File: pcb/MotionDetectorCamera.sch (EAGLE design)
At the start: 127 parts, among them J2 S-MOUNT-LENS-HOLDER, U1 LATTICE-ICE40HX4K-BG121, U10 NXP-NTB0102, U11 ON-NLAS3157, U12 ON-NLAS3157, U13 STM-STM32F730, U2 TI-TPS6280XYKAR, U3 MICROSD-SOCKET, U4 TI-TPS6280XYKAR, U5 W989D6DBGX6I, U6 TI-TPS63805YFFR, U8 ON-AR0330CS1C12SPKA0, U9 TI-TMUX1574, X1 SITIME-SIT8021, X2 SITIME-SIT8021

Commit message: Commit before renaming ICE_PRG lines
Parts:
- C56: device EagleLibrary:CAPACITOR0402 -> EagleLibrary:CAPACITOR0805; MFG (none) -> Walsin; PN (none) -> 0805X475M250CT
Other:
- moved on the sheet: C22, H2, J2, LED0, LED1, LED2, LED3, R14, R16, R20, R22, TP6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

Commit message: Routing progress
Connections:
- removed net ICE_PRG_CDONE: H2.5, U1E.CDONE_K8
- removed net ICE_PRG_CLK: H2.2, U1E.SPI_SCK_L10
- removed net ICE_PRG_CRST_: H2.10, R5.2, U1E.CRESET_B_L9
- removed net ICE_PRG_CS_: H2.3, U1E.SPI_SS_B_K10
- removed net ICE_PRG_DI: H2.1, U1E.SPI_SI_J9
- removed net ICE_PRG_DO: H2.4, U1E.SPI_SO_K9
- removed net STM_SPI_CLK: U13B.PB2_M6
- removed net STM_SPI_CS_: U13B.PB6_B6
- removed net STM_SPI_D0: U13C.PC9_F14
- removed net STM_SPI_D1: U13C.PC10_B14
- removed net STM_SPI_D2: U13E.PE2_A2
- removed net STM_SPI_D3: U13F.PF6_K2
- removed net STM_SPI_D4: U13H.PH2_F4
- removed net STM_SPI_D5: U13H.PH3_G4
- removed net STM_SPI_D6: U13G.PG9_C10
- removed net STM_SPI_D7: U13G.PG14_A7
- new net ICE_CDONE: H2.5, U13I.PI7_C2, U1E.CDONE_K8
- new net ICE_CRST_: H2.10, R5.2, U13I.PI6_C3, U1E.CRESET_B_L9
- new net ICE_SPI_CLK: H2.2, U13B.PB2_M6, U1E.SPI_SCK_L10
- new net ICE_SPI_CS_: H2.3, U13B.PB6_B6, U1E.SPI_SS_B_K10
- new net ICE_SPI_D0: H2.1, U13C.PC9_F14, U1E.SPI_SI_J9
- new net ICE_SPI_D1: H2.4, U13C.PC10_B14, U1E.SPI_SO_K9
- new net ICE_SPI_D2: U13E.PE2_A2, U1C.J8
- new net ICE_SPI_D3: U13F.PF6_K2, U1C.L7
- new net ICE_SPI_D4: U13H.PH2_F4, U1C.J7
- new net ICE_SPI_D5: U13H.PH3_G4, U1C.K7
- new net ICE_SPI_D6: U13G.PG9_C10, U1C.H7
- new net ICE_SPI_D7: U13G.PG14_A7, U1C.L8
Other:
- moved on the sheet: C67, C68, R28, R29, R30, R31, U13J

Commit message: Layout progress
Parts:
- removed LED0: LED, EagleLibrary:LED
- removed R29, R30: 10k, EagleLibrary:RESISTOR0402
- added LED4: LED, EagleLibrary:LED
- C56: device EagleLibrary:CAPACITOR0805 -> EagleLibrary:CAPACITOR0603; MFG Walsin -> Taiyo Yuden; PN 0805X475M250CT -> LMK107BJ475KA-T
- C57, C58, C67: MFG (none) -> AVX; PN (none) -> 0402ZD225MAT2A
- C60, C66: MFG (none) -> Taiyo Yuden; PN (none) -> EMK105BJ105MVHF
- H1: value WURTH-61201021621 -> HEADER-2X5; device EagleLibrary:WURTH-61201021621 -> EagleLibrary:HEADER-2X5
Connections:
- net N$15 renamed STM_BOOT
- net N$19 renamed STM_RST_
- removed net N$22: R29.2, U13J.PDR_ON_C6
- removed net N$24: R30.2, U13J.BYPASS_REG_L4
- net 1V8: now also U13J.PDR_ON_C6; no longer R29.1
- net GND: now also U13J.BYPASS_REG_L4; no longer R30.1
- net ICE_LED0: now also LED1.A; no longer LED0.A
- net ICE_LED1: now also LED2.A; no longer LED1.A
- net ICE_LED2: now also LED3.A; no longer LED2.A
- net ICE_LED3: now also LED4.A; no longer LED3.A
- net N$23: now also LED1.C; no longer LED0.C
- net N$26: now also LED2.C; no longer LED1.C
- net N$29: now also LED3.C; no longer LED2.C
- net N$31: now also LED4.C; no longer LED3.C
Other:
- moved on the sheet: C68, LED1, LED2, LED3, LED5, LED6, LED7, LED8, R15, R17, R31, R32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

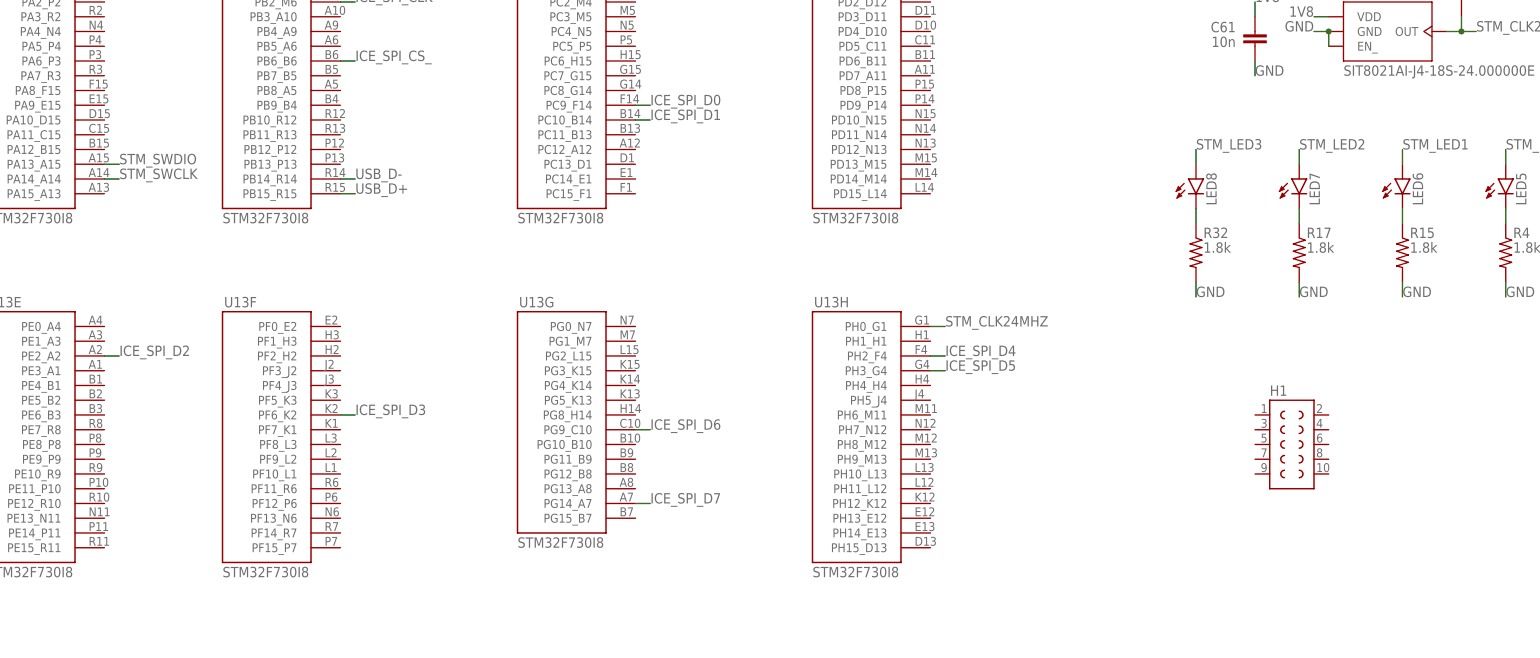
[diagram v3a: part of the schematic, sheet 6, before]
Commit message: Wired up STM32 LEDs
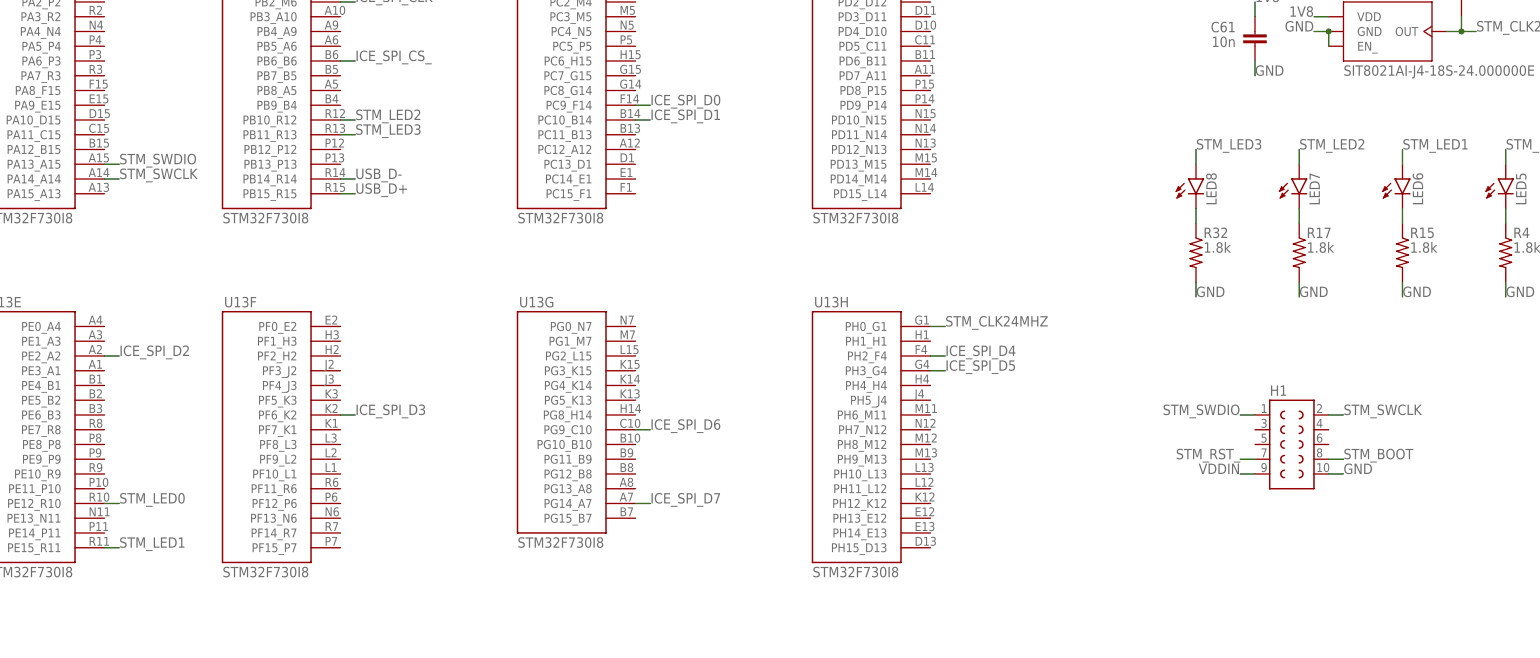
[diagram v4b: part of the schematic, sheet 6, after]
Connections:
- net GND: now also H1.10
- net STM_BOOT: now also H1.8
- net STM_LED0: now also U13E.PE12_R10
- net STM_LED1: now also U13E.PE15_R11
- net STM_LED2: now also U13B.PB10_R12
- net STM_LED3: now also U13B.PB11_R13
- net STM_RST_: now also H1.7
- net STM_SWCLK: now also H1.2
- net STM_SWDIO: now also H1.1
- net VDDIN: now also H1.9
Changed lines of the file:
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@@
 <label x="81.28" y="-142.24" size="1.778" layer="95"/>
+</segment>
+<segment>
+<pinref part="H1" gate="G$1" pin="10"/>
+<wire x1="238.76" y1="-99.06" x2="241.3" y2="-99.06" width="0.1524" layer="91"/>
+<label x="241.3" y="-99.06" size="1.778" layer="95"/>
 </segment>
 </net>
@@
 <label x="101.6" y="-144.78" size="1.778" layer="95"/>
 </segment>
+<segment>
+<pinref part="H1" gate="G$1" pin="7"/>
+<wire x1="226.06" y1="-96.52" x2="223.52" y2="-96.52" width="0.1524" layer="91"/>
+<label x="223.52" y="-96.52" size="1.778" layer="95" align="bottom-right"/>
+</segment>
 </net>
 <net name="STM_BOOT" class="0">
@@
 <junction x="116.84" y="-139.7"/>
 </segment>
+<segment>
+<pinref part="H1" gate="G$1" pin="8"/>
+<wire x1="238.76" y1="-96.52" x2="241.3" y2="-96.52" width="0.1524" layer="91"/>
+<label x="241.3" y="-96.52" size="1.778" layer="95"/>
+</segment>
 </net>
 <net name="USB_D-" class="0">
@@
 <label x="30.48" y="-45.72" size="1.778" layer="95"/>
 </segment>
+<segment>
+<pinref part="H1" gate="G$1" pin="1"/>
+<wire x1="226.06" y1="-88.9" x2="223.52" y2="-88.9" width="0.1524" layer="91"/>
+<label x="223.52" y="-88.9" size="1.778" layer="95" align="bottom-right"/>
+</segment>
 </net>
 <net name="STM_SWCLK" class="0">
@@
 <wire x1="27.94" y1="-48.26" x2="30.48" y2="-48.26" width="0.1524" layer="91"/>
 <label x="30.48" y="-48.26" size="1.778" layer="95"/>
+</segment>
+<segment>
+<pinref part="H1" gate="G$1" pin="2"/>
+<wire x1="238.76" y1="-88.9" x2="241.3" y2="-88.9" width="0.1524" layer="91"/>
+<label x="241.3" y="-88.9" size="1.778" layer="95"/>
 </segment>
 </net>
@@
 <label x="269.24" y="-43.18" size="1.778" layer="95"/>
 </segment>
+<segment>
+<pinref part="U13" gate="E" pin="PE12_R10"/>
+<wire x1="27.94" y1="-104.14" x2="30.48" y2="-104.14" width="0.1524" layer="91"/>
+<label x="30.48" y="-104.14" size="1.778" layer="95"/>
+</segment>
 </net>
 <net name="STM_LED1" class="0">
@@
 <label x="251.46" y="-43.18" size="1.778" layer="95"/>
 </segment>
+<segment>
+<pinref part="U13" gate="E" pin="PE15_R11"/>
+<wire x1="27.94" y1="-111.76" x2="30.48" y2="-111.76" width="0.1524" layer="91"/>
+<label x="30.48" y="-111.76" size="1.778" layer="95"/>
+</segment>
 </net>
 <net name="STM_LED2" class="0">
@@
 <label x="233.68" y="-43.18" size="1.778" layer="95"/>
 </segment>
+<segment>
+<pinref part="U13" gate="B" pin="PB10_R12"/>
+<wire x1="68.58" y1="-38.1" x2="71.12" y2="-38.1" width="0.1524" layer="91"/>
+<label x="71.12" y="-38.1" size="1.778" layer="95"/>
+</segment>
 </net>
 <net name="STM_LED3" class="0">
@@
 <label x="215.9" y="-43.18" size="1.778" layer="95"/>
 </segment>
+<segment>
+<pinref part="U13" gate="B" pin="PB11_R13"/>
+<wire x1="68.58" y1="-40.64" x2="71.12" y2="-40.64" width="0.1524" layer="91"/>
+<label x="71.12" y="-40.64" size="1.778" layer="95"/>
+</segment>
 </net>
 <net name="ICE_CDONE" class="0">
@@
 </segment>
 </net>
+<net name="VDDIN" class="0">
+<segment>
+<pinref part="H1" gate="G$1" pin="9"/>
+<wire x1="226.06" y1="-99.06" x2="223.52" y2="-99.06" width="0.1524" layer="91"/>
+<label x="223.52" y="-99.06" size="1.778" layer="95" align="bottom-right"/>
+</segment>
+</net>

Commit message: Laying out SD card in progress
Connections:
- net ICE_SD_CLK: now also U1C.L3
- net ICE_SD_DAT0: now also U1C.L2; no longer U1C.L3
- net ICE_SD_DAT1: now also U1C.L1; no longer U1C.K4
- net ICE_SD_DAT2: now also U1C.K4; no longer U1C.L1
- net ICE_SD_DAT3: no longer U1C.L2
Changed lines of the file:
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@@
 <label x="152.4" y="30.48" size="1.778" layer="95"/>
 </segment>
-</net>
-<net name="ICE_SD_CMD" class="0">
-<segment>
-<pinref part="U1" gate="C" pin="K3"/>
-<wire x1="149.86" y1="48.26" x2="152.4" y2="48.26" width="0.1524" layer="91"/>
-<label x="152.4" y="48.26" size="1.778" layer="95"/>
-</segment>
-</net>
-<net name="ICE_SD_DAT0" class="0">
 <segment>
 <pinref part="U1" gate="C" pin="L3"/>
 <wire x1="149.86" y1="60.96" x2="152.4" y2="60.96" width="0.1524" layer="91"/>
 <label x="152.4" y="60.96" size="1.778" layer="95"/>
-</segment>
-</net>
-<net name="ICE_SD_DAT1" class="0">
-<segment>
-<pinref part="U1" gate="C" pin="K4"/>
-<wire x1="149.86" y1="45.72" x2="152.4" y2="45.72" width="0.1524" layer="91"/>
-<label x="152.4" y="45.72" size="1.778" layer="95"/>
-</segment>
-</net>
-<net name="ICE_SD_DAT2" class="0">
-<segment>
-<pinref part="U1" gate="C" pin="L1"/>
-<wire x1="149.86" y1="66.04" x2="152.4" y2="66.04" width="0.1524" layer="91"/>
-<label x="152.4" y="66.04" size="1.778" layer="95"/>
-</segment>
-</net>
-<net name="ICE_SD_DAT3" class="0">
-<segment>
-<pinref part="U1" gate="C" pin="L2"/>
-<wire x1="149.86" y1="63.5" x2="152.4" y2="63.5" width="0.1524" layer="91"/>
-<label x="152.4" y="63.5" size="1.778" layer="95"/>
 </segment>
 </net>
@@
 </segment>
 </net>
+<net name="ICE_SD_DAT1" class="0">
+<segment>
+<pinref part="U1" gate="C" pin="L1"/>
+<wire x1="149.86" y1="66.04" x2="152.4" y2="66.04" width="0.1524" layer="91"/>
+<label x="152.4" y="66.04" size="1.778" layer="95"/>
+</segment>
+</net>
+<net name="ICE_SD_DAT2" class="0">
+<segment>
+<pinref part="U1" gate="C" pin="K4"/>
+<wire x1="149.86" y1="45.72" x2="152.4" y2="45.72" width="0.1524" layer="91"/>
+<label x="152.4" y="45.72" size="1.778" layer="95"/>
+</segment>
+</net>
+<net name="ICE_SD_DAT0" class="0">
+<segment>
+<pinref part="U1" gate="C" pin="L2"/>
+<wire x1="149.86" y1="63.5" x2="152.4" y2="63.5" width="0.1524" layer="91"/>
+<label x="152.4" y="63.5" size="1.778" layer="95"/>
+</segment>
+</net>
+<net name="ICE_SD_CMD" class="0">
+<segment>
+<pinref part="U1" gate="C" pin="K3"/>
+<wire x1="149.86" y1="48.26" x2="152.4" y2="48.26" width="0.1524" layer="91"/>
+<label x="152.4" y="48.26" size="1.778" layer="95"/>
+</segment>
+</net>

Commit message: Layout progress
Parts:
- added C30, C31, C62, C63, C64: 100n, EagleLibrary:CAPACITOR0402
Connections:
- net 1V8: now also C30.1
- net 2V8: now also C31.1, C62.1, C63.1, C64.1
- net GND: now also C30.2, C31.2, C62.2, C63.2, C64.2
- net ICE_SD_CLK: now also U1C.K3; no longer U1C.J5, U1C.L3
- net ICE_SD_CMD: now also U1C.L3; no longer U1C.K3
- net ICE_SD_DAT2: now also U1C.L4, U9.S4A; no longer U1C.K4, U9.S3A
- net ICE_SD_DAT3: now also U1C.K4, U9.S3A; no longer U9.S4A
- net ICE_SD_INIT: now also U1C.L5
- net N$17: now also U9.S4B; no longer U9.S3B
- net N$21: now also U9.S3B; no longer U9.S4B
- net SD_DAT0: now also U9.D2; no longer U9.D1
- net SD_DAT1: now also U9.D1; no longer U9.D2
- net SD_DAT2: now also U9.D4; no longer U9.D3
- net SD_DAT3: now also U9.D3; no longer U9.D4
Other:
- moved on the sheet: C19, C20, R26, R27, U3

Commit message: Layout progress
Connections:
- net ICE_SD_CLK: now also U1C.K4; no longer U1C.K3
- net ICE_SD_DAT1: now also U1C.K3; no longer U1C.L1
- net ICE_SD_DAT2: now also U1C.L5; no longer U1C.L4
- net ICE_SD_DAT3: now also U1C.L4; no longer U1C.K4
- net ICE_SD_INIT: now also U1C.L1; no longer U1C.L5
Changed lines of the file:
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@@
 <net name="ICE_SD_CLK" class="0">
 <segment>
-<pinref part="U1" gate="C" pin="K3"/>
-<wire x1="149.86" y1="48.26" x2="152.4" y2="48.26" width="0.1524" layer="91"/>
-<label x="152.4" y="48.26" size="1.778" layer="95"/>
+<wire x1="149.86" y1="45.72" x2="152.4" y2="45.72" width="0.1524" layer="91"/>
+<label x="152.4" y="45.72" size="1.778" layer="95"/>
+<pinref part="U1" gate="C" pin="K4"/>
 </segment>
 </net>
@@
 <net name="ICE_SD_DAT1" class="0">
 <segment>
-<pinref part="U1" gate="C" pin="L1"/>
-<wire x1="149.86" y1="66.04" x2="152.4" y2="66.04" width="0.1524" layer="91"/>
-<label x="152.4" y="66.04" size="1.778" layer="95"/>
+<wire x1="149.86" y1="48.26" x2="152.4" y2="48.26" width="0.1524" layer="91"/>
+<label x="152.4" y="48.26" size="1.778" layer="95"/>
+<pinref part="U1" gate="C" pin="K3"/>
 </segment>
 </net>
 <net name="ICE_SD_DAT0" class="0">
 <segment>
-<pinref part="U1" gate="C" pin="L2"/>
 <wire x1="149.86" y1="63.5" x2="152.4" y2="63.5" width="0.1524" layer="91"/>
 <label x="152.4" y="63.5" size="1.778" layer="95"/>
+<pinref part="U1" gate="C" pin="L2"/>
 </segment>
 </net>
 <net name="ICE_SD_CMD" class="0">
 <segment>
-<pinref part="U1" gate="C" pin="L3"/>
 <wire x1="149.86" y1="60.96" x2="152.4" y2="60.96" width="0.1524" layer="91"/>
 <label x="152.4" y="60.96" size="1.778" layer="95"/>
+<pinref part="U1" gate="C" pin="L3"/>
 </segment>
 </net>
 <net name="ICE_SD_DAT2" class="0">
 <segment>
-<pinref part="U1" gate="C" pin="L4"/>
-<wire x1="149.86" y1="58.42" x2="152.4" y2="58.42" width="0.1524" layer="91"/>
-<label x="152.4" y="58.42" size="1.778" layer="95"/>
+<wire x1="149.86" y1="55.88" x2="152.4" y2="55.88" width="0.1524" layer="91"/>
+<label x="152.4" y="55.88" size="1.778" layer="95"/>
+<pinref part="U1" gate="C" pin="L5"/>
 </segment>
 </net>
 <net name="ICE_SD_DAT3" class="0">
 <segment>
-<pinref part="U1" gate="C" pin="K4"/>
-<wire x1="149.86" y1="45.72" x2="152.4" y2="45.72" width="0.1524" layer="91"/>
-<label x="152.4" y="45.72" size="1.778" layer="95"/>
+<wire x1="149.86" y1="58.42" x2="152.4" y2="58.42" width="0.1524" layer="91"/>
+<label x="152.4" y="58.42" size="1.778" layer="95"/>
+<pinref part="U1" gate="C" pin="L4"/>
 </segment>
 </net>
 <net name="ICE_SD_INIT" class="0">
 <segment>
-<pinref part="U1" gate="C" pin="L5"/>
-<wire x1="149.86" y1="55.88" x2="152.4" y2="55.88" width="0.1524" layer="91"/>
-<label x="152.4" y="55.88" size="1.778" layer="95"/>
+<wire x1="149.86" y1="66.04" x2="152.4" y2="66.04" width="0.1524" layer="91"/>
+<label x="152.4" y="66.04" size="1.778" layer="95"/>
+<pinref part="U1" gate="C" pin="L1"/>
 </segment>
 </net>

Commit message: Layout progress
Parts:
- removed H2: WURTH-61201021621, EagleLibrary:WURTH-61201021621
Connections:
- removed net N$35: H2.9
- net 1V8: no longer H2.7
- net GND: no longer H2.8
- net ICE_CDONE: no longer H2.5
- net ICE_CRST_: no longer H2.10
- net ICE_SPI_CLK: no longer H2.2
- net ICE_SPI_CS_: no longer H2.3
- net ICE_SPI_D0: no longer H2.1
- net ICE_SPI_D1: no longer H2.4
- net VDDIN: no longer H2.6
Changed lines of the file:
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@@
 <attribute name="PN" value="CRGP0402F1K8"/>
 </part>
-<part name="H2" library="EagleLibrary" deviceset="WURTH-61201021621" device="" package3d_urn="urn:adsk.eagle:package:19109748/1"/>
 <part name="H1" library="EagleLibrary" deviceset="HEADER-2X5" device=""/>
 <part name="C30" library="EagleLibrary" deviceset="CAPACITOR" device="0402" package3d_urn="urn:adsk.eagle:package:17080064/1" value="100n">
@@
 <attribute name="NAME" x="193.04" y="-73.66" size="1.778" layer="95" rot="R180"/>
 </instance>
-<instance part="H2" gate="G$1" x="172.72" y="-114.3" smashed="yes">
-<attribute name="NAME" x="172.72" y="-113.538" size="1.778" layer="95"/>
-</instance>
 </instances>
 <busses>
@@
 <wire x1="167.64" y1="-83.82" x2="165.1" y2="-83.82" width="0.1524" layer="91"/>
 <label x="165.1" y="-83.82" size="1.778" layer="95" align="bottom-right"/>
-</segment>
-<segment>
-<pinref part="H2" gate="G$1" pin="7"/>
-<wire x1="182.88" y1="-119.38" x2="185.42" y2="-119.38" width="0.1524" layer="91"/>
-<label x="185.42" y="-119.38" size="1.778" layer="95"/>
 </segment>
 </net>
@@
 <label x="154.94" y="-93.98" size="1.778" layer="95"/>
 </segment>
-<segment>
-<pinref part="H2" gate="G$1" pin="8"/>
-<wire x1="170.18" y1="-119.38" x2="167.64" y2="-119.38" width="0.1524" layer="91"/>
-<label x="167.64" y="-119.38" size="1.778" layer="95" align="bottom-right"/>
-</segment>
 </net>
 <net name="ICE_PIX_CLK24MHZ" class="0">
@@
 <wire x1="76.2" y1="-111.76" x2="73.66" y2="-111.76" width="0.1524" layer="91"/>
 </segment>
-<segment>
-<pinref part="H2" gate="G$1" pin="5"/>
-<wire x1="182.88" y1="-121.92" x2="185.42" y2="-121.92" width="0.1524" layer="91"/>
-<label x="185.42" y="-121.92" size="1.778" layer="95"/>
-</segment>
 </net>
 <net name="ICE_CRST_" class="0">
@@
 <wire x1="81.28" y1="-129.54" x2="81.28" y2="-96.52" width="0.1524" layer="91"/>
 </segment>
-<segment>
-<pinref part="H2" gate="G$1" pin="10"/>
-<wire x1="170.18" y1="-116.84" x2="167.64" y2="-116.84" width="0.1524" layer="91"/>
-<label x="167.64" y="-116.84" size="1.778" layer="95" align="bottom-right"/>
-</segment>
 </net>
 <net name="ICE_SPI_D1" class="0">
@@
 <label x="80.772" y="-83.82" size="1.778" layer="95" rot="MR0"/>
 </segment>
-<segment>
-<pinref part="H2" gate="G$1" pin="4"/>
-<wire x1="170.18" y1="-124.46" x2="167.64" y2="-124.46" width="0.1524" layer="91"/>
-<label x="167.64" y="-124.46" size="1.778" layer="95" align="bottom-right"/>
-</segment>
 </net>
 <net name="ICE_SPI_D0" class="0">
@@
 <label x="80.772" y="-81.28" size="1.778" layer="95" rot="MR0"/>
 </segment>
-<segment>
-<pinref part="H2" gate="G$1" pin="1"/>
-<wire x1="182.88" y1="-127" x2="185.42" y2="-127" width="0.1524" layer="91"/>
-<label x="185.42" y="-127" size="1.778" layer="95"/>
-</segment>
 </net>
 <net name="ICE_SPI_CLK" class="0">
@@
 <label x="80.772" y="-88.9" size="1.778" layer="95" rot="MR0"/>
 </segment>
-<segment>
-<pinref part="H2" gate="G$1" pin="2"/>
-<wire x1="170.18" y1="-127" x2="167.64" y2="-127" width="0.1524" layer="91"/>
-<label x="167.64" y="-127" size="1.778" layer="95" align="bottom-right"/>
-</segment>
 </net>
 <net name="ICE_SPI_CS_" class="0">
@@
 <wire x1="86.36" y1="-86.36" x2="81.28" y2="-86.36" width="0.1524" layer="91"/>
 <label x="80.772" y="-86.36" size="1.778" layer="95" rot="MR0"/>
-</segment>
-<segment>
-<pinref part="H2" gate="G$1" pin="3"/>
-<wire x1="182.88" y1="-124.46" x2="185.42" y2="-124.46" width="0.1524" layer="91"/>
-<label x="185.42" y="-124.46" size="1.778" layer="95"/>
 </segment>
 </net>
@@
 </segment>
 </net>
-<net name="N$35" class="0">
-<segment>
-<pinref part="H2" gate="G$1" pin="9"/>
-<wire x1="182.88" y1="-116.84" x2="185.42" y2="-116.84" width="0.1524" layer="91"/>
-</segment>
-</net>
-<net name="VDDIN" class="0">
-<segment>
-<pinref part="H2" gate="G$1" pin="6"/>
-<wire x1="170.18" y1="-121.92" x2="167.64" y2="-121.92" width="0.1524" layer="91"/>
-<label x="167.64" y="-121.92" size="1.778" layer="95" align="bottom-right"/>
-</segment>
-</net>
